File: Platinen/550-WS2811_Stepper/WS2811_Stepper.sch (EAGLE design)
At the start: 50 parts, among them CON1 End SW1, CON2 End SW2, CON3 End SW1H, CON4 STEPPER_CON, CON5 End SW2H, CON6 NEMA17, CON7 LED, IC1 4017N, J10 MiniStp1, M1 BOARD_A4988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

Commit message: 6-pin Stepper Conector
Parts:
- J10: value MiniStp1 -> (none); device Pfostenstecker_4_u_6:CON-HARTING-ML_ML4 -> con-harting-ml:ML6
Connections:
- removed net N$15: C3.1, CON7.2, JP1.3, JP2.3, JP3.3, R5.1, U2R.OUTB, U3H.OUTB
- new net LED: C3.1, CON7.2, J10.6, JP1.3, JP2.3, JP3.3, R5.1, U2R.OUTB, U3H.OUTB
- net +5V: now also J10.5
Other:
- note added: "Bei einem kleinen Stepper reichen 100uF"
- note added: "Winzige Stepper für Signale oder Weichen. Wenn keine LED benutzt wird, dann 4-pol Stecker"
- note removed: "Winzige Stepper für Signale oder Weichen"

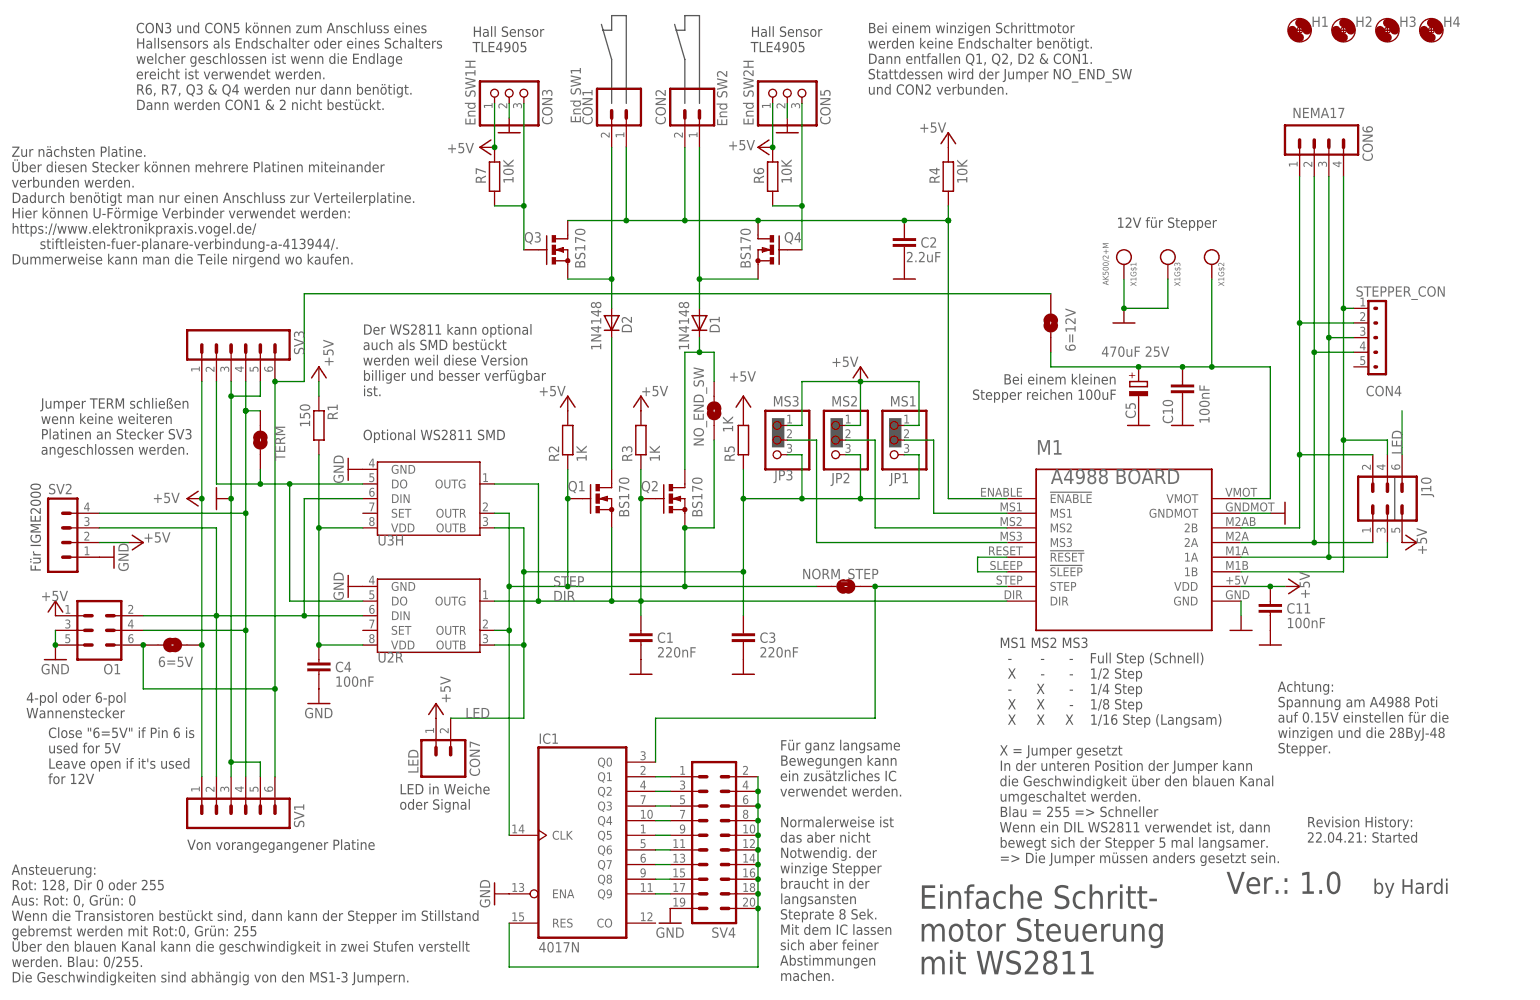
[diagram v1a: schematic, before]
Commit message: Corrected 6=12V Jumper
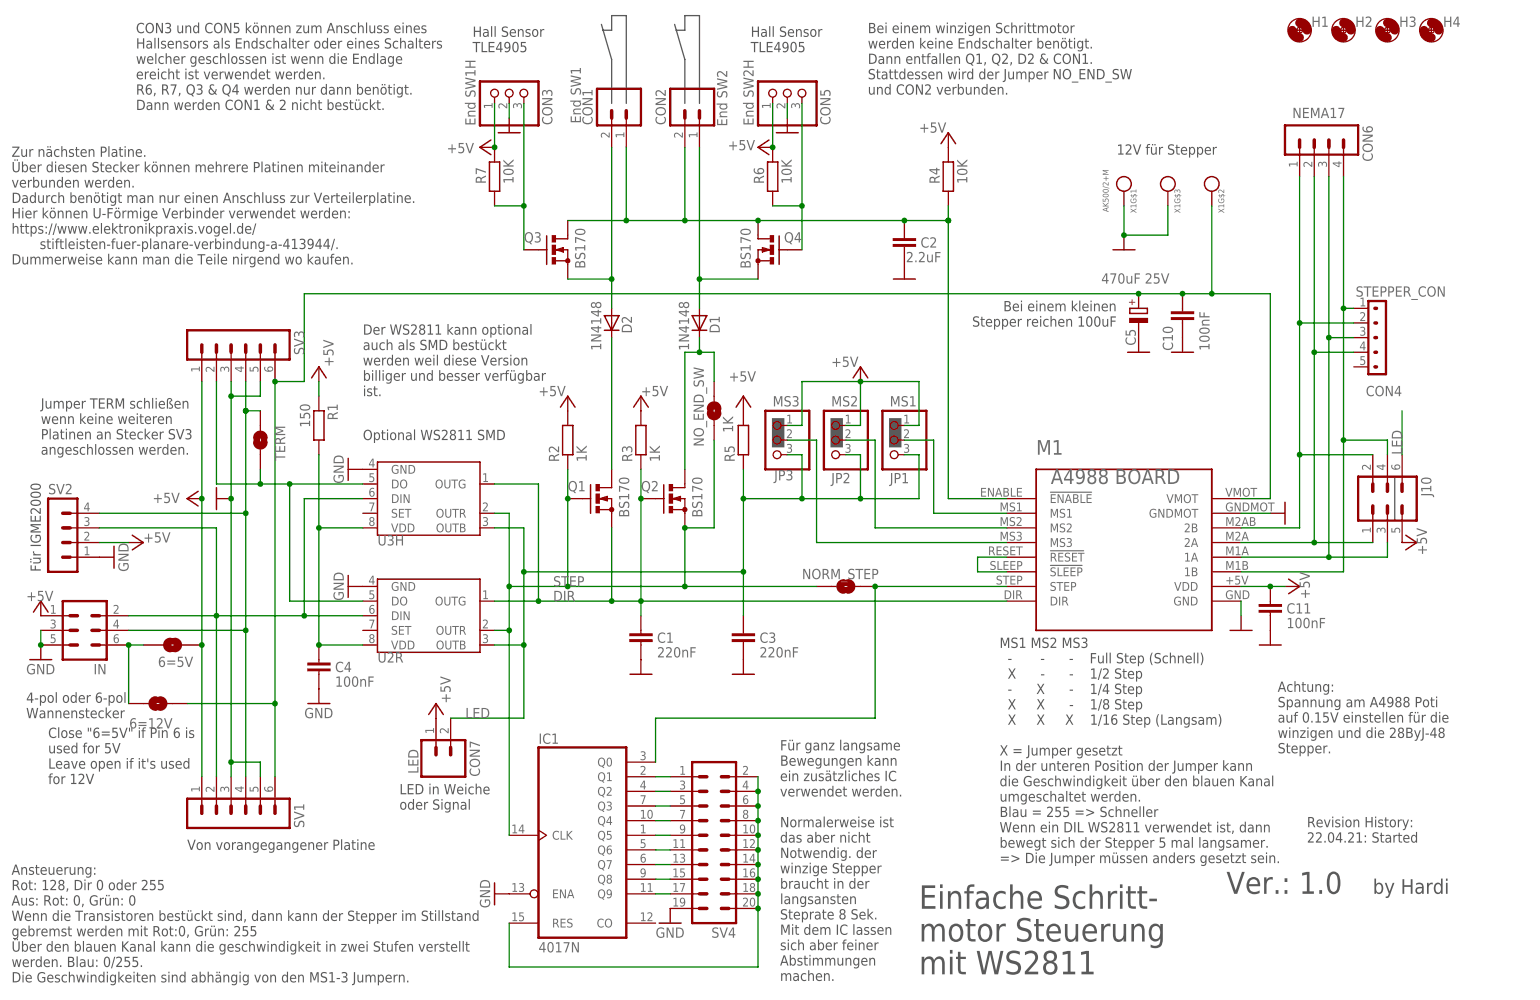
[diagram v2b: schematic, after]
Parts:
- removed O1: (no value), con-harting-ml:ML6
- added IN: (no value), con-harting-ml:ML6
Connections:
- removed net N$12: 6=12V.2, C10.1, C5.+, M1.VMOT, X1G$2.KL
- new net N$15: 6=12V.2, 6=5V.1, IN.6
- net +5V: now also IN.1; no longer O1.1
- net GND: now also IN.3, IN.5; no longer O1.3, O1.5
- net N$2: now also IN.2; no longer O1.2
- net N$4: now also IN.4; no longer O1.4
- net N$7: now also C10.1, C5.+, M1.VMOT, X1G$2.KL; no longer 6=5V.1, O1.6
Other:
- moved on the sheet: 6=12V, C10, C5, X1G$1, X1G$2, X1G$3
